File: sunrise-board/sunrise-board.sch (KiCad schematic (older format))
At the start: 30 parts, among them J1 Barrel Jack 12V, J2 FTDI Basic, J3 Header, J4 LED_STRIP_VGRB, J5 I2C, J6 Header, Q1 IRLZ34N, Q2 IRLZ34N, Q3 IRLZ34N, SW1 Reset, U1 L4931CZ50-AP, U2 ATmega328P-PU, U3 DS1307+, Y1 16MHz, Y2 32.768Hz

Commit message: print the schematic
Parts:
- renumbered J3 to J2, J2 to J3, J6 to J4, J4 to J5, J5 to J6, R3 to R1, R4 to R2, R5 to R3, R1 to R4, R6 to R5, R7 to R6, R2 to R7, U3 to U2, U2 to U3, Y2 to Y1, Y1 to Y2

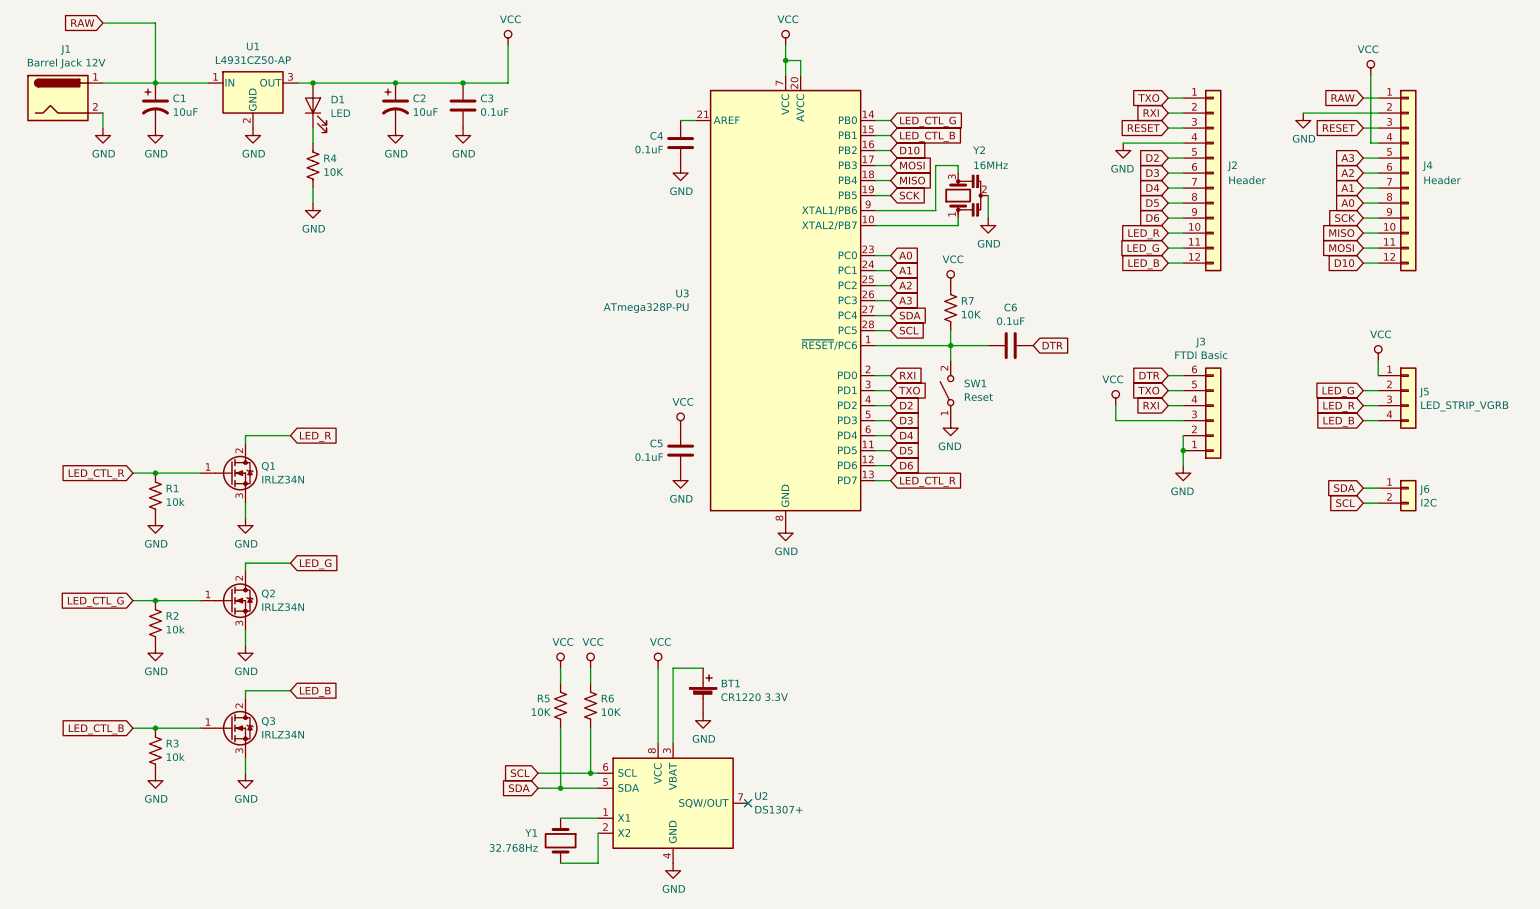
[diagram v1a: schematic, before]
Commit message: update schematic and assign some footprints
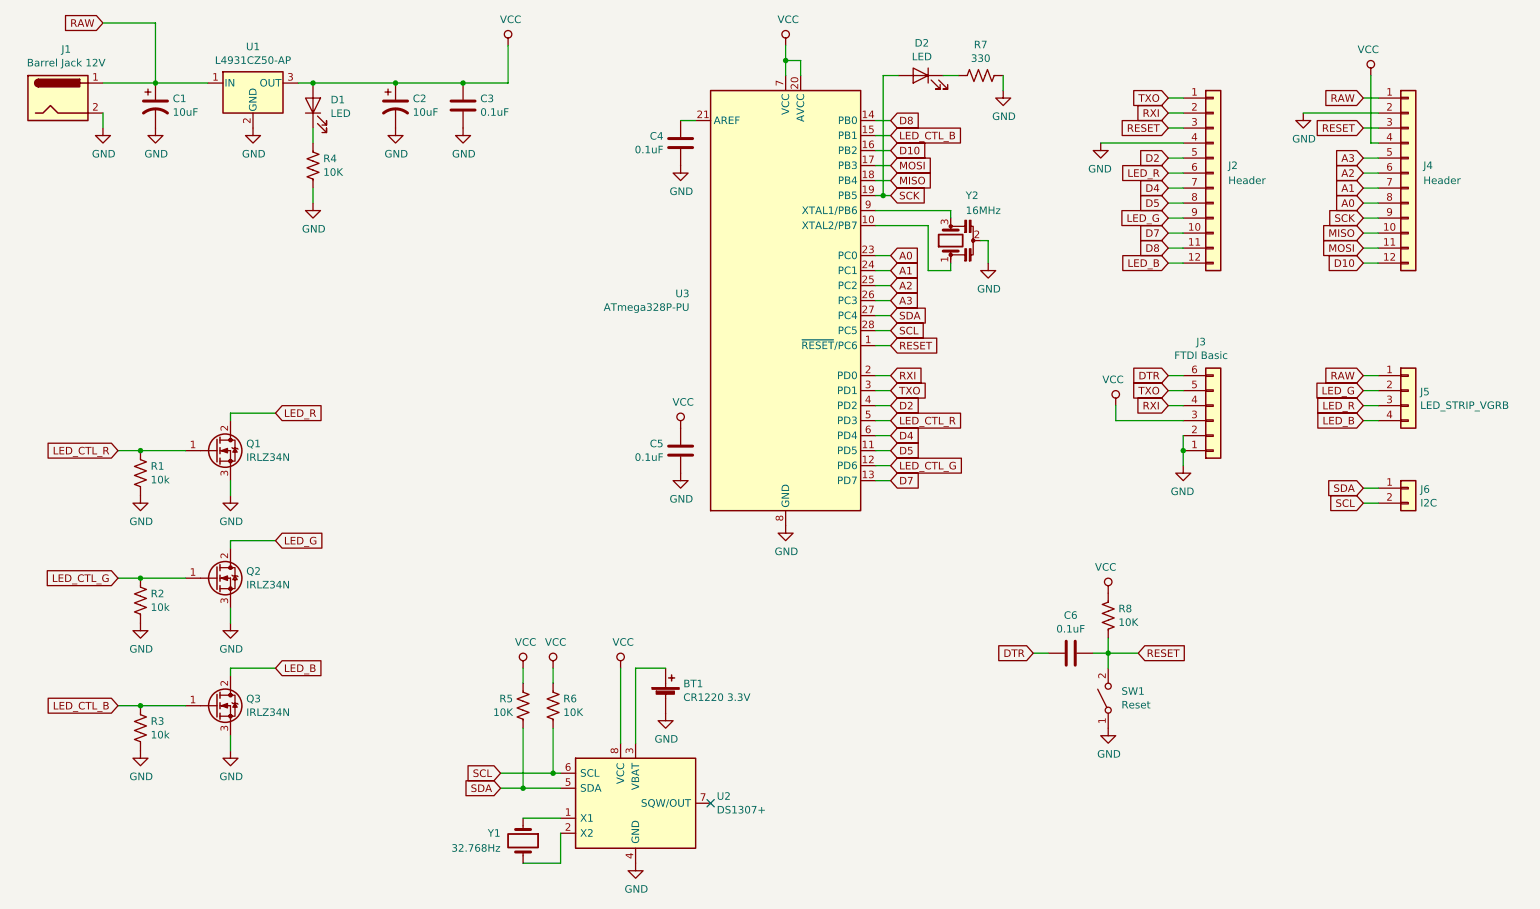
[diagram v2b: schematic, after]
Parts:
- added D2: LED, LED_THT:LED_D3.0mm, symbol Device:LED
- added R7: 330, Resistor_THT:R_Axial_DIN0207_L6.3mm_D2.5mm_P10.16mm_Horizontal, symbol Device:R_US
- D1: footprint (none) -> LED_THT:LED_D3.0mm
- J1: footprint (none) -> Connector_BarrelJack:BarrelJack_Horizontal
- J2, J4: footprint (none) -> Connector_PinHeader_2.54mm:PinHeader_1x12_P2.54mm_Vertical
- J3: footprint (none) -> Connector_PinHeader_2.54mm:PinHeader_1x06_P2.54mm_Vertical
- J5: footprint (none) -> Connector_PinHeader_2.54mm:PinHeader_1x04_P2.54mm_Vertical
- J6: footprint (none) -> Connector_PinHeader_2.54mm:PinHeader_1x02_P2.54mm_Vertical
- R1, R2, R3, R4, R5, R6: footprint (none) -> Resistor_THT:R_Axial_DIN0207_L6.3mm_D2.5mm_P10.16mm_Horizontal
- R8: renamed from R7; footprint (none) -> Resistor_THT:R_Axial_DIN0207_L6.3mm_D2.5mm_P10.16mm_Horizontal
- U1: footprint (none) -> Package_TO_SOT_THT:TO-92_Inline
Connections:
- net GND: now also R7.1
- net LED_CTL_G: now also U3.12 (PD6); no longer U3.14 (PB0)
- net LED_CTL_R: now also U3.5 (PD3); no longer U3.13 (PD7)
- net LED_G: now also J2.9 (Pin_9); no longer J2.11 (Pin_11)
- net LED_R: now also J2.6 (Pin_6); no longer J2.10 (Pin_10)
- net RAW: now also J5.1 (Pin_1)
- net RESET: now also C6.1, R8.2, SW1.2 (B), U3.1 (~RESET~/PC6)
- net SCK: now also D2.2 (A)
- net VCC: no longer J5.1 (Pin_1)
- removed net D3: J2.6 (Pin_6), U3.5 (PD3)
- removed net D6: J2.9 (Pin_9), U3.12 (PD6)
- new net: D2.1 (K), R7.2
- new net D7: J2.10 (Pin_10), U3.13 (PD7)
- new net D8: J2.11 (Pin_11), U3.14 (PB0)
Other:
- moved on the sheet: BT1, C6, Q1, Q2, Q3, R1, R2, R3, R5, R6, R8, SW1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

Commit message: finish assigning footprints
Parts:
- BT1: footprint (none) -> Sunrise:BatteryHolder_CR1220_THT
- C1, C2: footprint (none) -> Capacitor_THT:CP_Radial_D4.0mm_P1.50mm
- C3, C4, C5, C6: footprint (none) -> Capacitor_THT:C_Disc_D4.7mm_W2.5mm_P5.00mm
- R1, R2, R3, R4, R5, R6, R7, R8: footprint Resistor_THT:R_Axial_DIN0207_L6.3mm_D2.5mm_P10.16mm_Horizontal -> Resistor_THT:R_Axial_DIN0207_L6.3mm_D2.5mm_P7.62mm_Horizontal
- SW1: footprint (none) -> Button_Switch_THT:SW_PUSH_6mm
- U1: footprint Package_TO_SOT_THT:TO-92_Inline -> Package_TO_SOT_THT:TO-92_Inline_Wide
- Y1: footprint (none) -> Crystal:Crystal_C26-LF_D2.1mm_L6.5mm_Horizontal_1EP_style2
- Y2: footprint (none) -> Crystal:Resonator-3Pin_W6.0mm_H3.0mm
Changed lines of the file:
@@
 F 0 "R1" H 1968 4196 50  0000 L CNN
 F 1 "10k" H 1968 4105 50  0000 L CNN
-F 2 "Resistor_THT:R_Axial_DIN0207_L6.3mm_D2.5mm_P10.16mm_Horizontal" V 1940 4140 50  0001 C CNN
+F 2 "Resistor_THT:R_Axial_DIN0207_L6.3mm_D2.5mm_P7.62mm_Horizontal" V 1940 4140 50  0001 C CNN
 F 3 "~" H 1900 4150 50  0001 C CNN
 	1    1900 4150
@@
 F 0 "R2" H 1968 5046 50  0000 L CNN
 F 1 "10k" H 1968 4955 50  0000 L CNN
-F 2 "Resistor_THT:R_Axial_DIN0207_L6.3mm_D2.5mm_P10.16mm_Horizontal" V 1940 4990 50  0001 C CNN
+F 2 "Resistor_THT:R_Axial_DIN0207_L6.3mm_D2.5mm_P7.62mm_Horizontal" V 1940 4990 50  0001 C CNN
 F 3 "~" H 1900 5000 50  0001 C CNN
 	1    1900 5000
@@
 F 0 "R3" H 1968 5896 50  0000 L CNN
 F 1 "10k" H 1968 5805 50  0000 L CNN
-F 2 "Resistor_THT:R_Axial_DIN0207_L6.3mm_D2.5mm_P10.16mm_Horizontal" V 1940 5840 50  0001 C CNN
+F 2 "Resistor_THT:R_Axial_DIN0207_L6.3mm_D2.5mm_P7.62mm_Horizontal" V 1940 5840 50  0001 C CNN
 F 3 "~" H 1900 5850 50  0001 C CNN
 	1    1900 5850
@@
 F 0 "Y1" V 4400 6450 50  0000 R CNN
 F 1 "32.768Hz" V 4500 6450 50  0000 R CNN
-F 2 "" H 4450 6600 50  0001 C CNN
+F 2 "Crystal:Crystal_C26-LF_D2.1mm_L6.5mm_Horizontal_1EP_style2" H 4450 6600 50  0001 C CNN
 F 3 "~" H 4450 6600 50  0001 C CNN
 	1    4450 6600
@@
 F 0 "C4" H 5386 1996 50  0000 R CNN
 F 1 "0.1uF" H 5386 1905 50  0000 R CNN
-F 2 "" H 5538 1800 50  0001 C CNN
+F 2 "Capacitor_THT:C_Disc_D4.7mm_W2.5mm_P5.00mm" H 5538 1800 50  0001 C CNN
 F 3 "~" H 5500 1950 50  0001 C CNN
 	1    5500 1950
@@
 F 0 "BT1" H 5518 5746 50  0000 L CNN
 F 1 "CR1220 3.3V" H 5518 5655 50  0000 L CNN
-F 2 "" V 5400 5710 50  0001 C CNN
+F 2 "Sunrise:BatteryHolder_CR1220_THT" V 5400 5710 50  0001 C CNN
 F 3 "~" V 5400 5710 50  0001 C CNN
 	1    5400 5650
@@
 F 0 "C5" H 5386 4046 50  0000 R CNN
 F 1 "0.1uF" H 5386 3955 50  0000 R CNN
-F 2 "" H 5538 3850 50  0001 C CNN
+F 2 "Capacitor_THT:C_Disc_D4.7mm_W2.5mm_P5.00mm" H 5538 3850 50  0001 C CNN
 F 3 "~" H 5500 4000 50  0001 C CNN
 	1    5500 4000
@@
 Wire Wire Line
 	4450 6250 4300 6250
-Text GLabel 1650 1150 0    50   Input ~ 0
-RAW
 $Comp
 L Device:CP1 C1
@@
 F 0 "C1" H 2115 1746 50  0000 L CNN
 F 1 "10uF" H 2115 1655 50  0000 L CNN
-F 2 "" H 2000 1700 50  0001 C CNN
+F 2 "Capacitor_THT:CP_Radial_D4.0mm_P1.50mm" H 2000 1700 50  0001 C CNN
 F 3 "~" H 2000 1700 50  0001 C CNN
 	1    2000 1700
@@
 F 0 "C3" H 4165 1746 50  0000 L CNN
 F 1 "0.1uF" H 4165 1655 50  0000 L CNN
-F 2 "" H 4088 1550 50  0001 C CNN
+F 2 "Capacitor_THT:C_Disc_D4.7mm_W2.5mm_P5.00mm" H 4088 1550 50  0001 C CNN
 F 3 "~" H 4050 1700 50  0001 C CNN
 	1    4050 1700
@@
 Wire Wire Line
 	2000 1550 2000 1150
-Wire Wire Line
-	2000 1150 1650 1150
 Connection ~ 2000 1550
 $Comp
@@
 F 0 "U1" H 2650 1792 50  0000 C CNN
 F 1 "L4931CZ50-AP" H 2650 1701 50  0000 C CNN
-F 2 "Package_TO_SOT_THT:TO-92_Inline" H 2675 1400 50  0001 L CIN
+F 2 "Package_TO_SOT_THT:TO-92_Inline_Wide" H 2675 1400 50  0001 L CIN
 F 3 "https://www.st.com/resource/en/datasheet/l4931.pdf" H 2650 1500 50  0001 C CNN
 	1    2650 1550
@@
 F 0 "C2" H 3715 1746 50  0000 L CNN
 F 1 "10uF" H 3715 1655 50  0000 L CNN
-F 2 "" H 3600 1700 50  0001 C CNN
+F 2 "Capacitor_THT:CP_Radial_D4.0mm_P1.50mm" H 3600 1700 50  0001 C CNN
 F 3 "~" H 3600 1700 50  0001 C CNN
 	1    3600 1700
@@
 F 0 "SW1" V 8396 5562 50  0000 R CNN
 F 1 "Reset" V 8305 5562 50  0000 R CNN
-F 2 "" H 8350 5650 50  0001 C CNN
+F 2 "Button_Switch_THT:SW_PUSH_6mm" H 8350 5650 50  0001 C CNN
 F 3 "" H 8350 5650 50  0001 C CNN
 	1    8350 5650
@@
 F 0 "R4" H 3118 2146 50  0000 L CNN
 F 1 "10K" H 3118 2055 50  0000 L CNN
-F 2 "Resistor_THT:R_Axial_DIN0207_L6.3mm_D2.5mm_P10.16mm_Horizontal" V 3090 2090 50  0001 C CNN
+F 2 "Resistor_THT:R_Axial_DIN0207_L6.3mm_D2.5mm_P7.62mm_Horizontal" V 3090 2090 50  0001 C CNN
 F 3 "~" H 3050 2100 50  0001 C CNN
 	1    3050 2100
@@
 F 0 "Y2" V 7600 2500 50  0000 R CNN
 F 1 "16MHz" V 7500 2500 50  0000 R CNN
-F 2 "" H 7275 2600 50  0001 C CNN
+F 2 "Crystal:Resonator-3Pin_W6.0mm_H3.0mm" H 7275 2600 50  0001 C CNN
 F 3 "~" H 7275 2600 50  0001 C CNN
 	1    7300 2600
@@
 F 0 "R6" H 4718 5746 50  0000 L CNN
 F 1 "10K" H 4718 5655 50  0000 L CNN
-F 2 "Resistor_THT:R_Axial_DIN0207_L6.3mm_D2.5mm_P10.16mm_Horizontal" V 4690 5690 50  0001 C CNN
+F 2 "Resistor_THT:R_Axial_DIN0207_L6.3mm_D2.5mm_P7.62mm_Horizontal" V 4690 5690 50  0001 C CNN
 F 3 "~" H 4650 5700 50  0001 C CNN
 	1    4650 5700
@@
 F 0 "R5" H 4383 5746 50  0000 R CNN
 F 1 "10K" H 4383 5655 50  0000 R CNN
-F 2 "Resistor_THT:R_Axial_DIN0207_L6.3mm_D2.5mm_P10.16mm_Horizontal" V 4490 5690 50  0001 C CNN
+F 2 "Resistor_THT:R_Axial_DIN0207_L6.3mm_D2.5mm_P7.62mm_Horizontal" V 4490 5690 50  0001 C CNN
 F 3 "~" H 4450 5700 50  0001 C CNN
 	1    4450 5700
@@
 F 0 "C6" V 7848 5350 50  0000 C CNN
 F 1 "0.1uF" V 7939 5350 50  0000 C CNN
-F 2 "" H 8138 5200 50  0001 C CNN
+F 2 "Capacitor_THT:C_Disc_D4.7mm_W2.5mm_P5.00mm" H 8138 5200 50  0001 C CNN
 F 3 "~" H 8100 5350 50  0001 C CNN
 	1    8100 5350
@@
 F 0 "R8" H 8282 5146 50  0000 R CNN
 F 1 "10K" H 8282 5055 50  0000 R CNN
-F 2 "Resistor_THT:R_Axial_DIN0207_L6.3mm_D2.5mm_P10.16mm_Horizontal" V 8390 5090 50  0001 C CNN
+F 2 "Resistor_THT:R_Axial_DIN0207_L6.3mm_D2.5mm_P7.62mm_Horizontal" V 8390 5090 50  0001 C CNN
 F 3 "~" H 8350 5100 50  0001 C CNN
 	1    8350 5100
@@
 F 0 "R7" V 7295 1500 50  0000 C CNN
 F 1 "330" V 7386 1500 50  0000 C CNN
-F 2 "Resistor_THT:R_Axial_DIN0207_L6.3mm_D2.5mm_P10.16mm_Horizontal" V 7540 1490 50  0001 C CNN
+F 2 "Resistor_THT:R_Axial_DIN0207_L6.3mm_D2.5mm_P7.62mm_Horizontal" V 7540 1490 50  0001 C CNN
 F 3 "~" H 7500 1500 50  0001 C CNN
 	1    7500 1500
@@
 Text GLabel 10050 3500 0    50   Input ~ 0
 RAW
+Wire Wire Line
+	2000 1150 1650 1150
+Text GLabel 1650 1150 0    50   Input ~ 0
+RAW
 $EndSCHEMATC
